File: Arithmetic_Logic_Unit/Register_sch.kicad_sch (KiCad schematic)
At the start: 19 parts, among them IC1 SN54173J, IC2 SN54173J, U1 74LS245

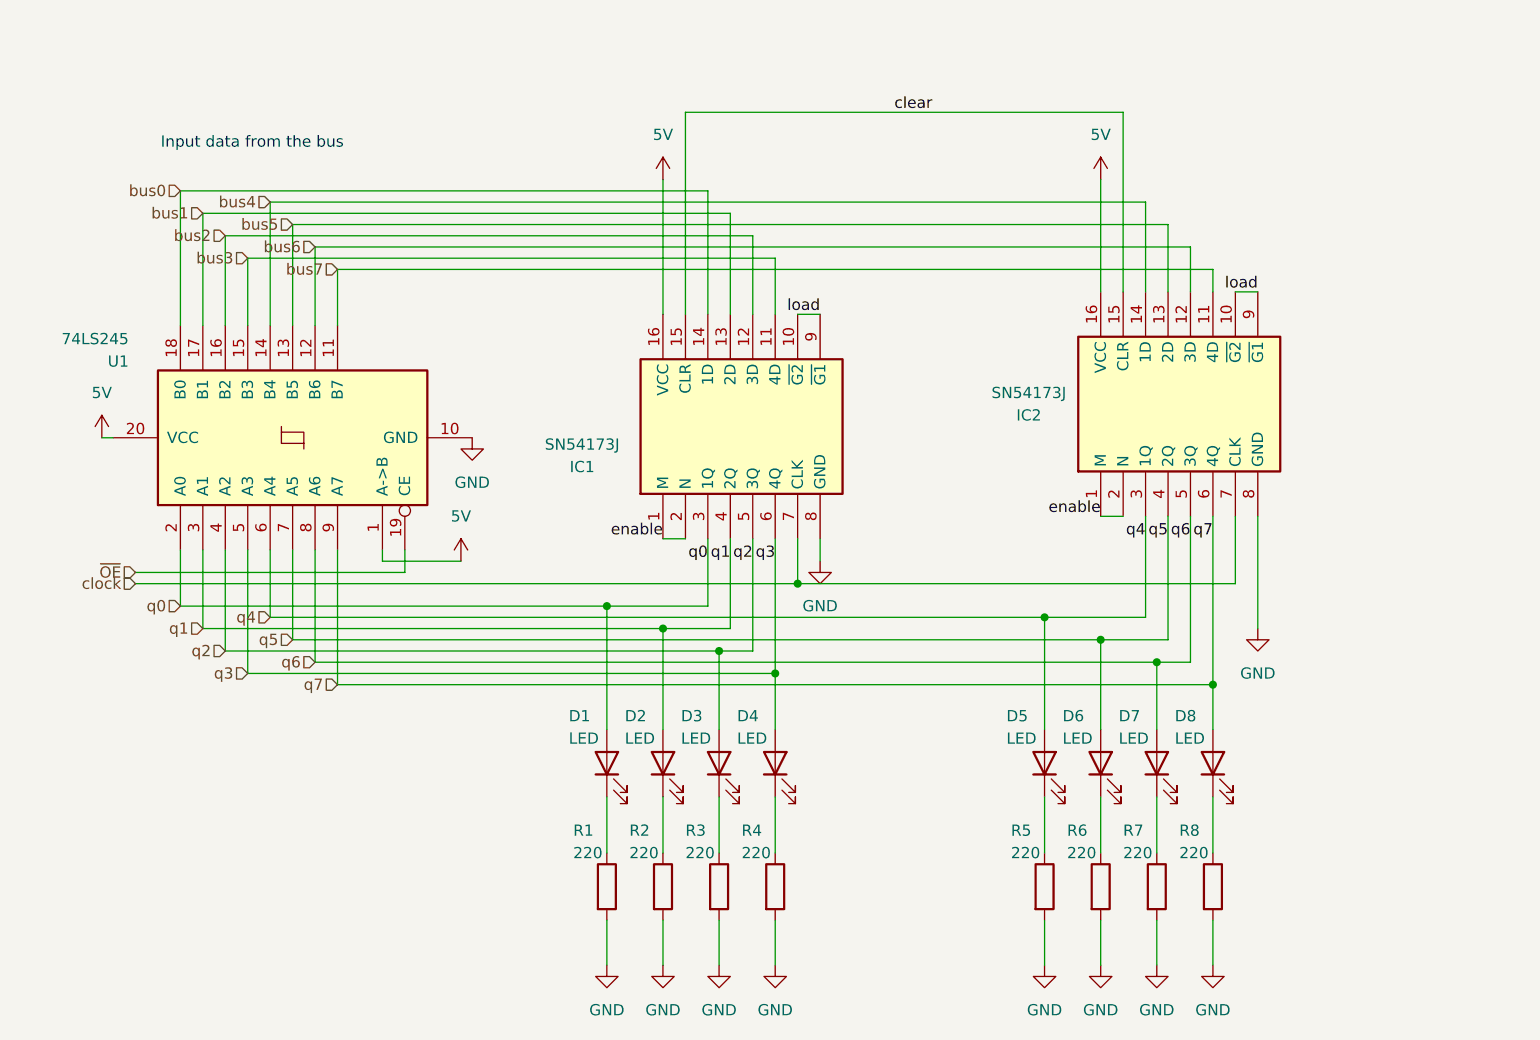
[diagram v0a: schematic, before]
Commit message: fixed incorrect footprint for sn54173
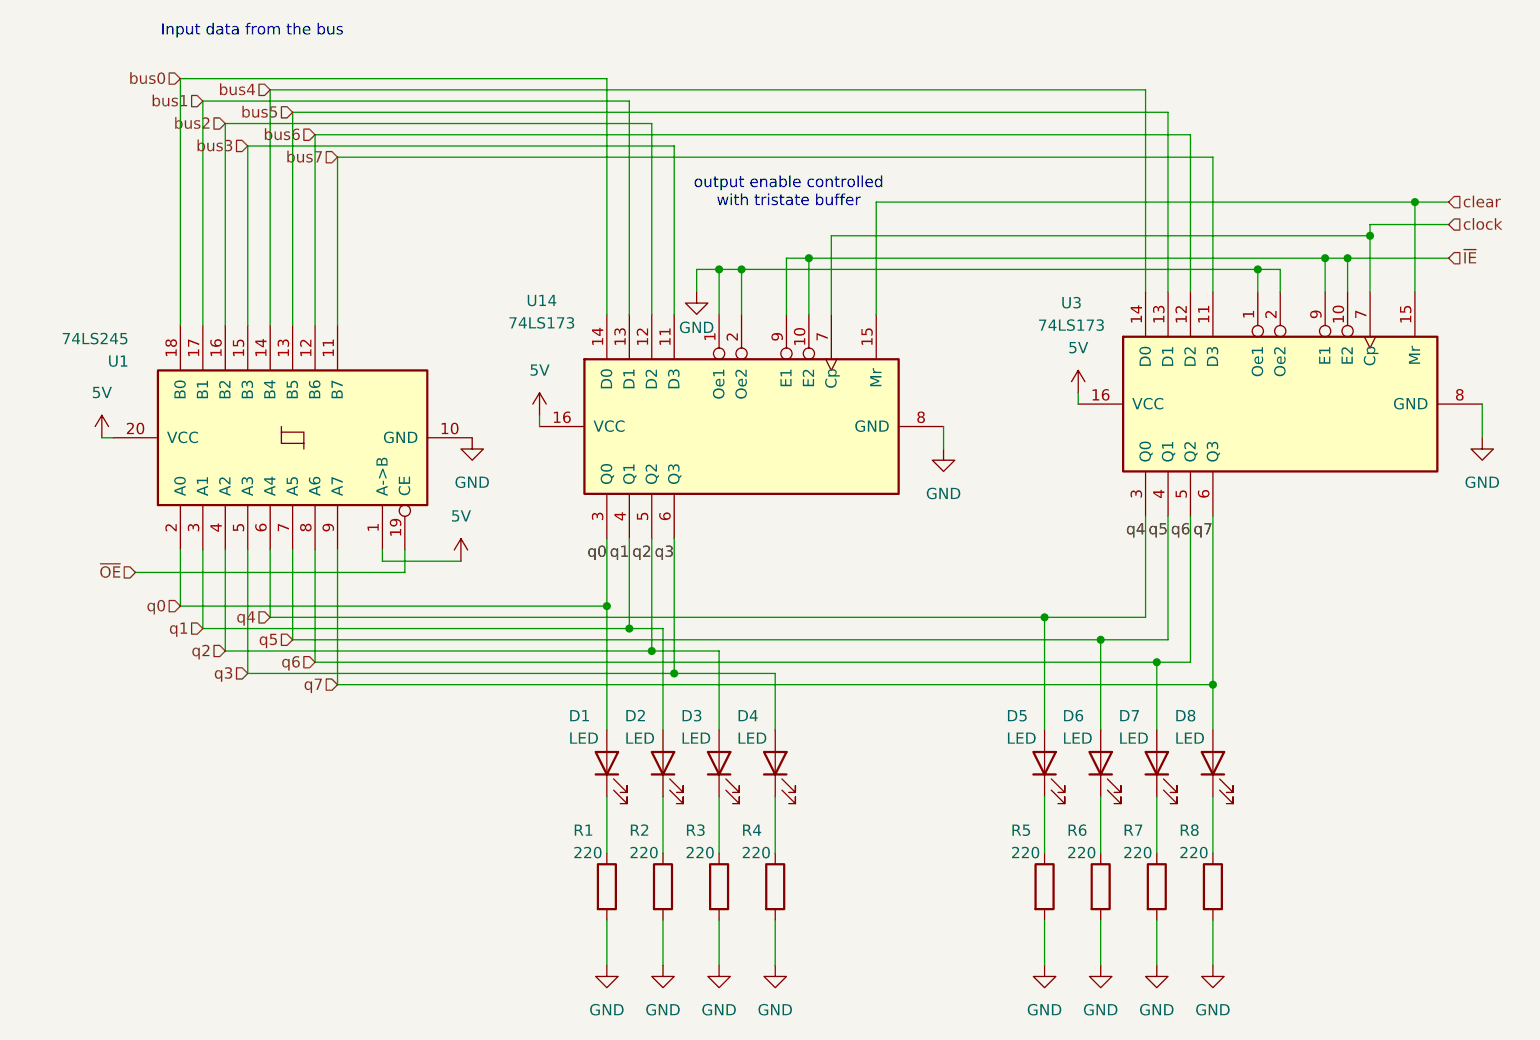
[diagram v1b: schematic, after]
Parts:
- removed IC1, IC2: SN54173J, footprints:SN54173J, symbol SN54173J:SN54173J
- added U14, U3: 74LS173, symbol 74xx:74LS173
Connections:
- net 5V: now also U14.16 (VCC), U3.16 (VCC)
- net GND: now also U14.1 (Oe1), U14.2 (Oe2), U14.8 (GND), U3.1 (Oe1), U3.2 (Oe2), U3.8 (GND)
- net bus0: now also U14.14 (D0)
- net bus1: now also U14.13 (D1)
- net bus2: now also U14.12 (D2)
- net bus3: now also U14.11 (D3)
- net bus4: now also U3.14 (D0)
- net bus5: now also U3.13 (D1)
- net bus6: now also U3.12 (D2)
- net bus7: now also U3.11 (D3)
- net clear: now also U14.15 (Mr), U3.15 (Mr)
- net clock: now also U14.7 (Cp), U3.7 (Cp)
- net q0: now also U14.3 (Q0)
- net q1: now also U14.4 (Q1)
- net q2: now also U14.5 (Q2)
- net q3: now also U14.6 (Q3)
- net q4: now also U3.3 (Q0)
- net q5: now also U3.4 (Q1)
- net q6: now also U3.5 (Q2)
- net q7: now also U3.6 (Q3)
- new net ~{IE}: U14.10 (E2), U14.9 (E1), U3.10 (E2), U3.9 (E1)
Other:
- note added: "output enable controlled with tristate buffer"

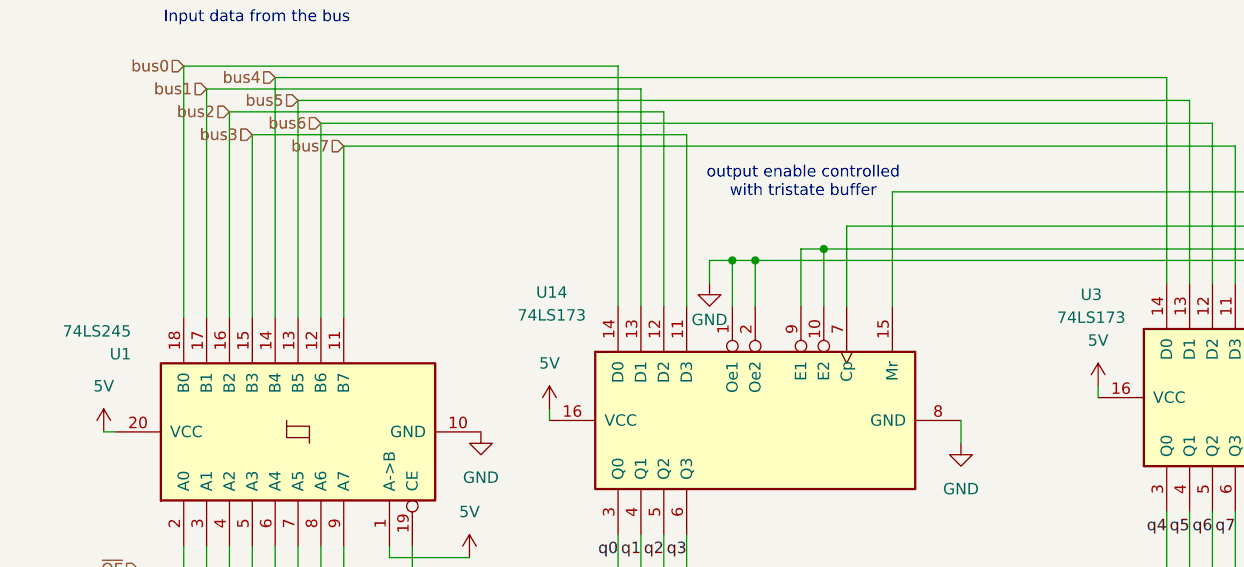
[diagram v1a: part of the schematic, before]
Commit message: fixed wiring issues
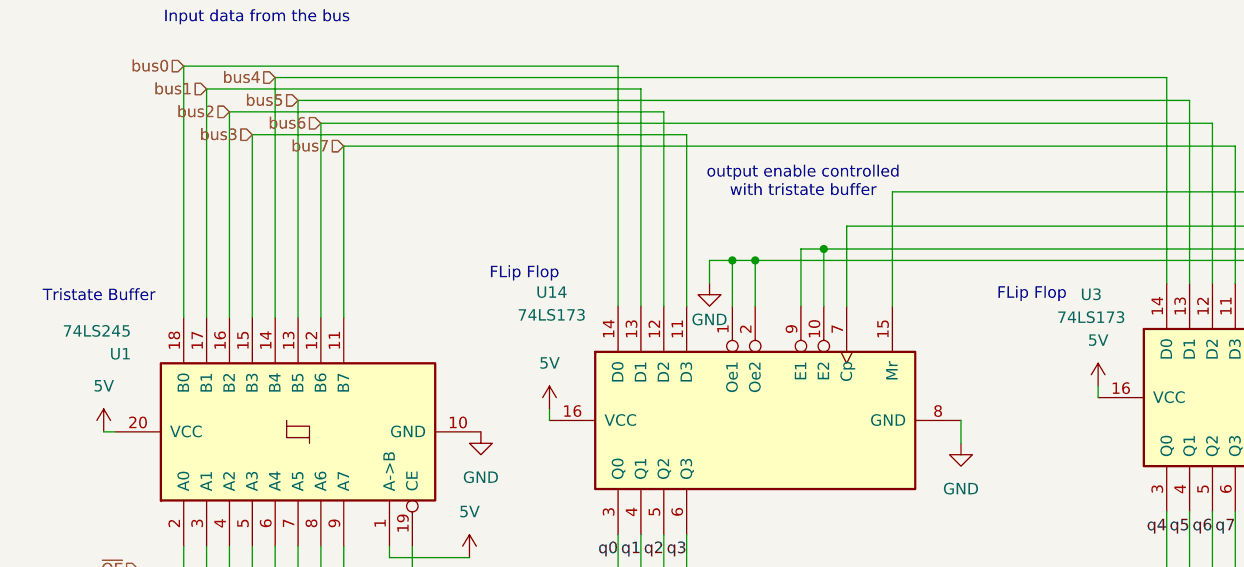
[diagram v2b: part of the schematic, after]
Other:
- note added: "FLip Flop"
- note added: "Tristate Buffer"
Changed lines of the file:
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@@
+		)
+	)
+	(text "FLip Flop"
+		(exclude_from_sim no)
+		(at 82.296 43.434 0)
+		(effects
+			(font
+				(size 1.27 1.27)
+			)
+		)
+	)
+	(text "FLip Flop"
+		(exclude_from_sim no)
+		(at 138.684 45.72 0)
+		(effects
+			(font
+				(size 1.27 1.27)
+			)
 		)
 	)
@@
 		(effects
 			(font
+				(size 1.27 1.27)
+			)
+		)
+	)
+	(text "Tristate Buffer"
+		(exclude_from_sim no)
+		(at 35.052 45.974 0)
+		(effects
+			(font

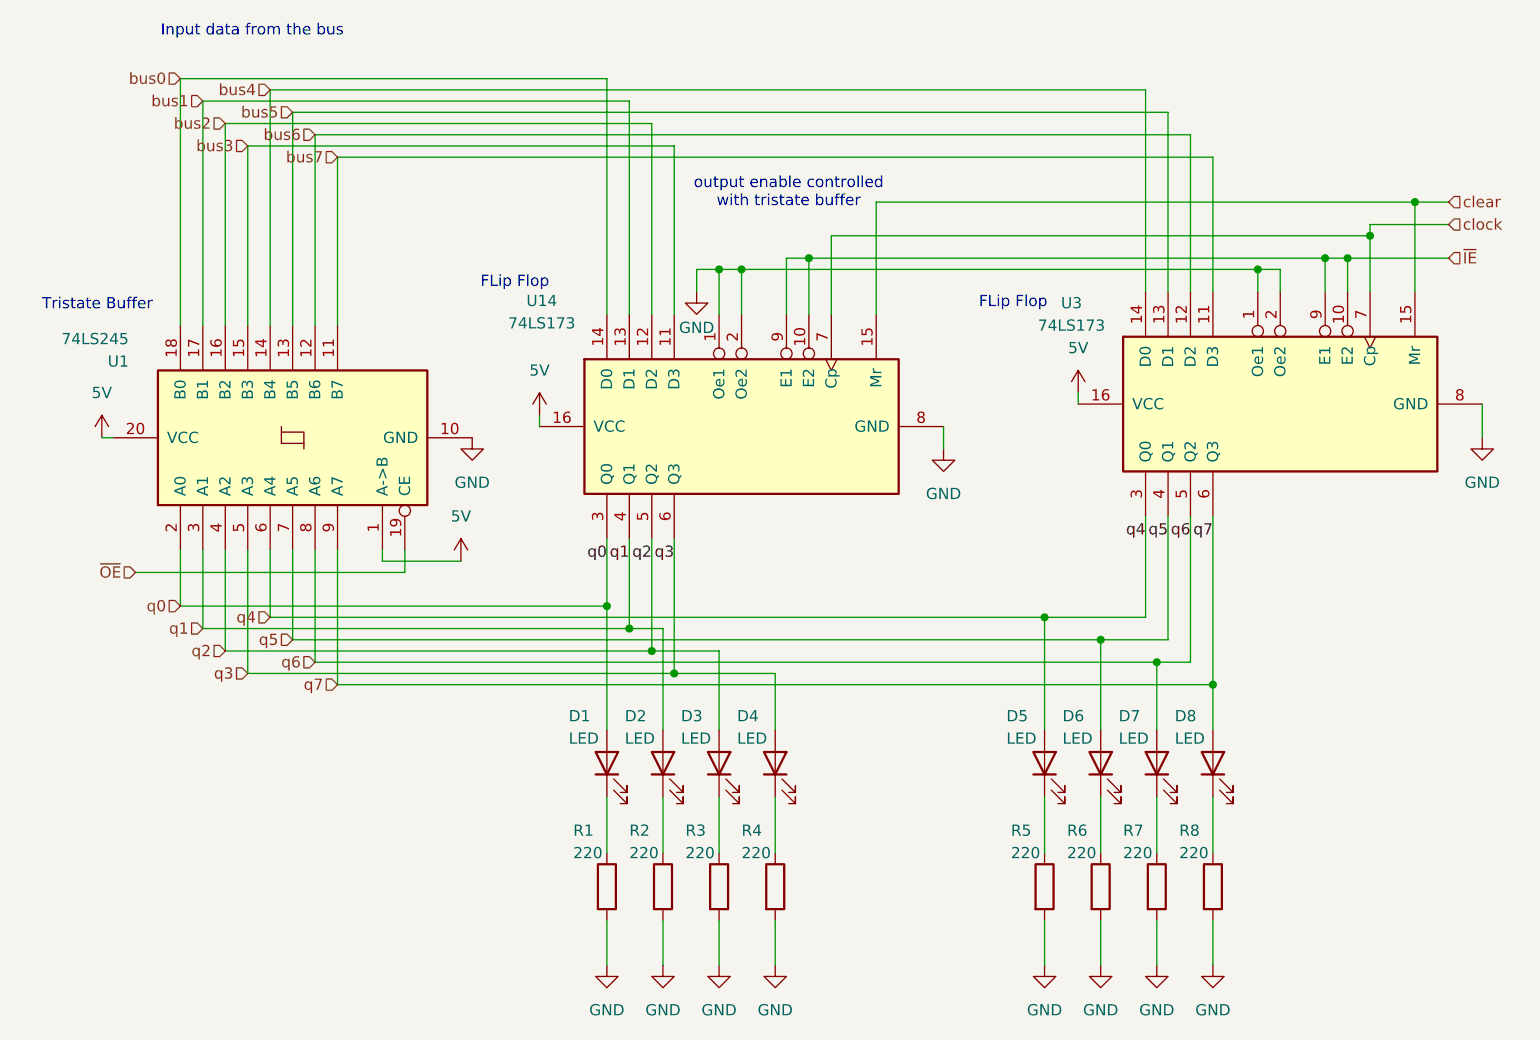
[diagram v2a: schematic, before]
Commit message: added bypass capacitors
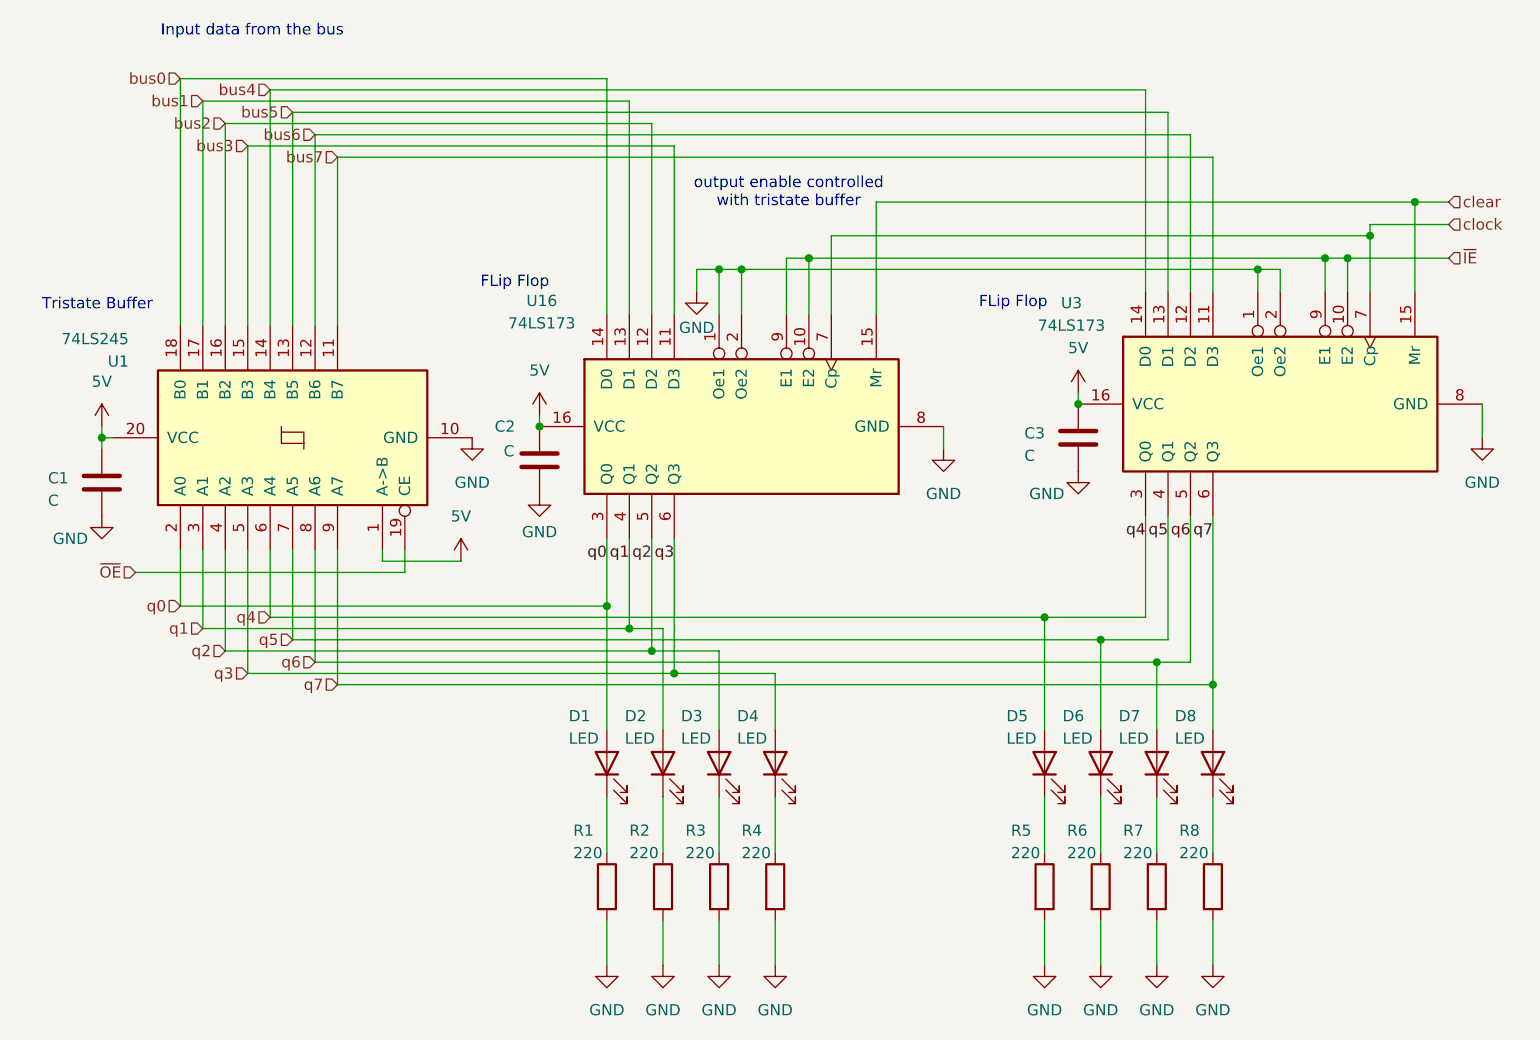
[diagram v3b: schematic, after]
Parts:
- added C1, C2, C3: C, symbol Device:C
- renumbered U14 to U16
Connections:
- net 5V: now also C1.2, C2.2, C3.2
- net GND: now also C1.1, C2.1, C3.1
